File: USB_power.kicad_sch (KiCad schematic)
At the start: 29 parts, among them J1 PWR_IN, J2 USB_A_Stacked, J3 Power_check, J4 USB_C_Receptacle_USB2.0_16P, J5 USB_A

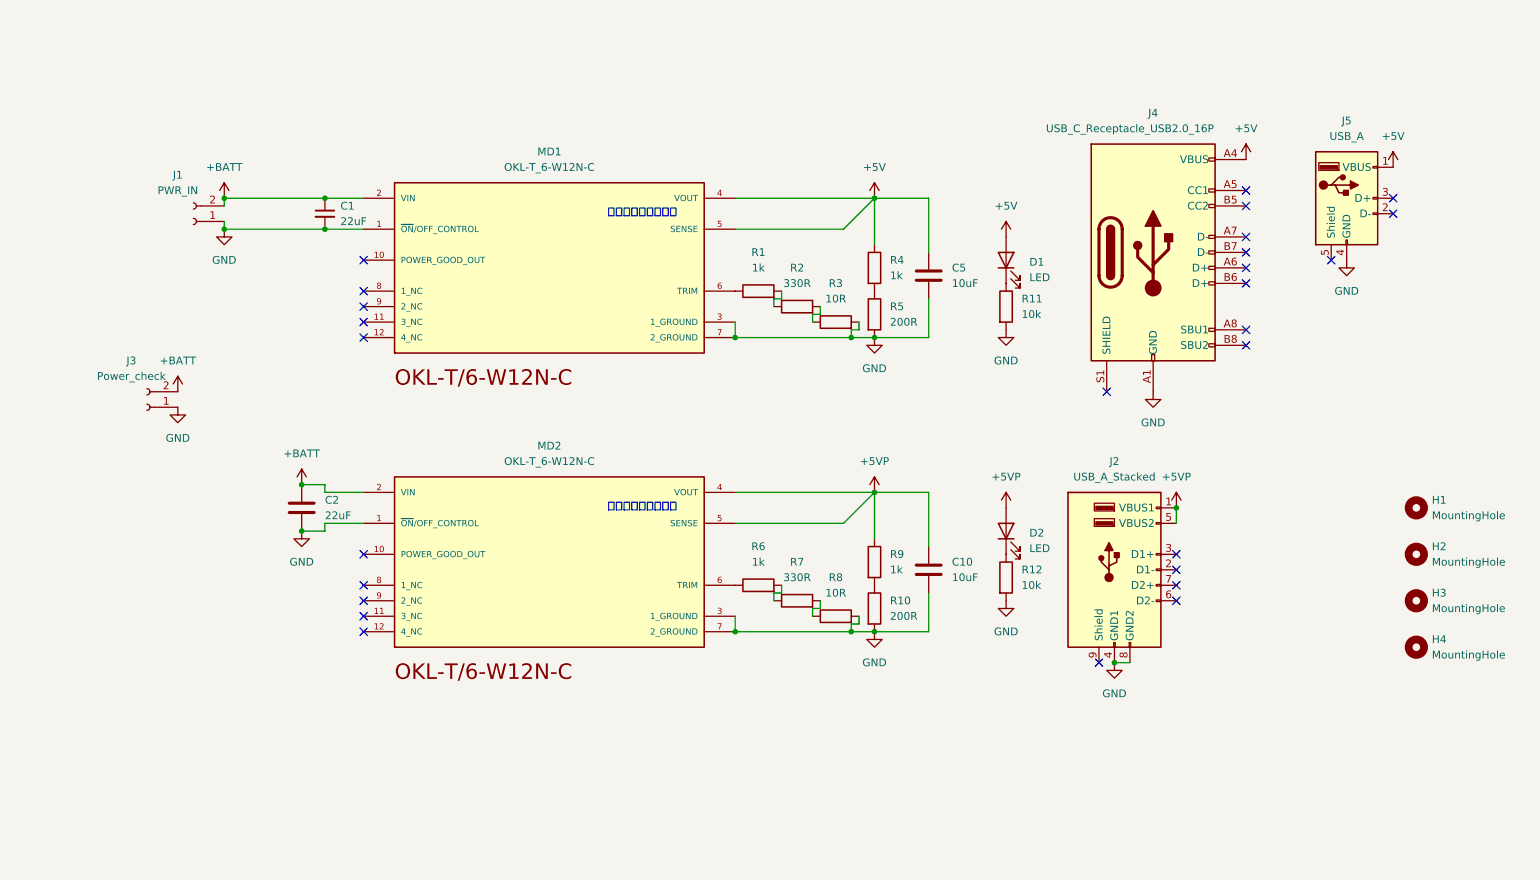
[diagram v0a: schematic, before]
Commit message: スケッチ見た目調整
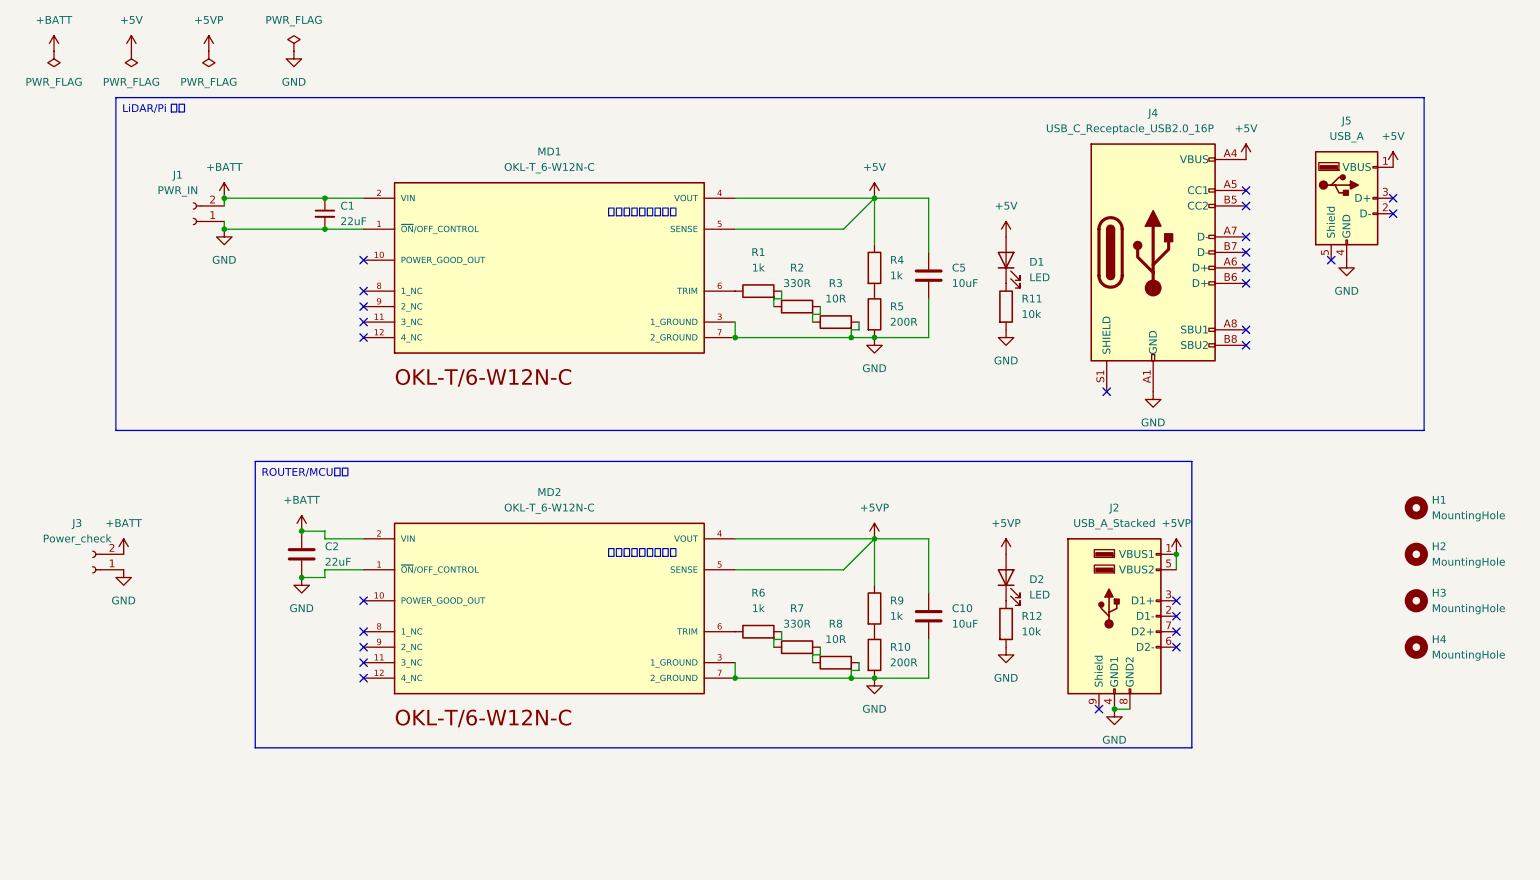
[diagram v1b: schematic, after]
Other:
- moved on the sheet: C10, C2, D2, J2, J3, MD2, R10, R12, R6, R7, R8, R9

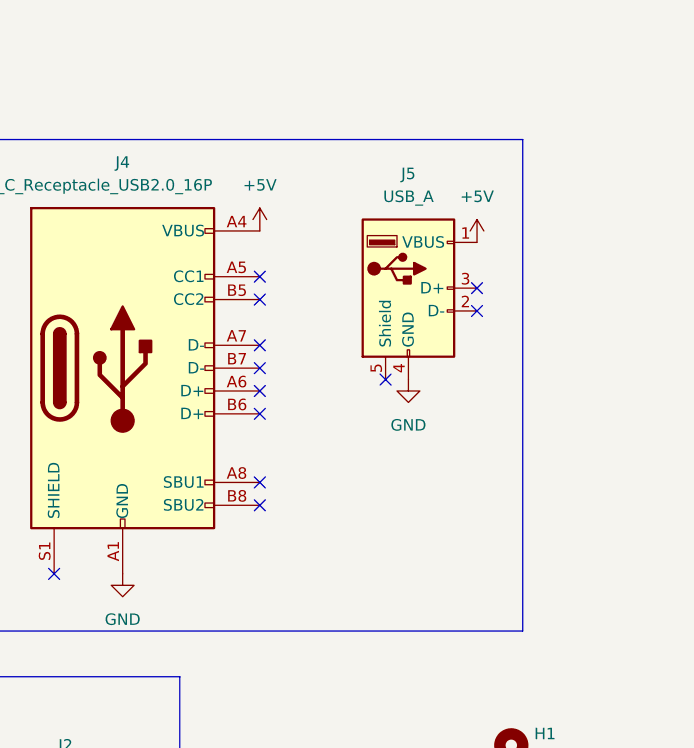
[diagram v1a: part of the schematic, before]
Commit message: SCH: MD1系統スタックコネクタに変更
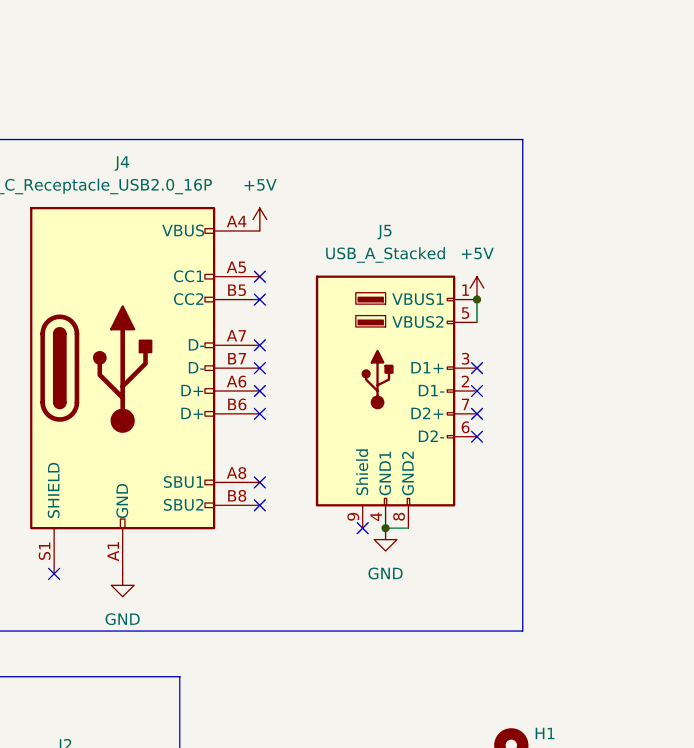
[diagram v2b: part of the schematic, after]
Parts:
- removed J5: USB_A, Connector_USB:USB_A_CONNFLY_DS1095-WNR0, symbol Connector:USB_A
- added J5: USB_A_Stacked, Connector_USB:USB_A_CUI_UJ2-ADH-TH_Horizontal_Stacked, symbol Connector:USB_A_Stacked
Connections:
- net +5V: now also J5.1 (VBUS1), J5.5 (VBUS2)
- net GND: now also J5.4 (GND1), J5.8 (GND2)
- no-connect marks 27 -> 29

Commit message: SCH: 不本意にもヒューズを追加
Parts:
- added F1: Fuse, FUSE_3557:FUSE_3557-2, symbol Device:Fuse
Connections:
- net +BATT: now also F1.1; no longer C1.1, MD1.2 (VIN)
- new net: C1.1, F1.2, MD1.2 (VIN)
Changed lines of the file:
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@@
+	)
+	(junction
+		(at 52.07 59.69)
+		(diameter 0)
+		(color 0 0 0 0)
 	)
 	(junction
@@
 	)
 	(junction
-		(at 52.07 59.69)
-		(diameter 0)
-		(color 0 0 0 0)
-	)
-	(junction
 		(at 64.77 121.92)
 		(diameter 0)
@@
 	)
 	(junction
-		(at 158.75 115.57)
+		(at 68.58 59.69)
 		(diameter 0)
 		(color 0 0 0 0)
 	)
 	(junction
-		(at 68.58 59.69)
+		(at 158.75 115.57)
 		(diameter 0)
 		(color 0 0 0 0)
@@
 	(wire
 		(pts
+			(xy 63.5 59.69) (xy 68.58 59.69)
+		)
+		(stroke
+			(width 0)
+			(type default)
+		)
+	)
+	(wire
+		(pts
 			(xy 167.64 76.2) (xy 167.64 82.55)
 		)
@@
 	(wire
 		(pts
-			(xy 52.07 59.69) (xy 68.58 59.69)
+			(xy 52.07 59.69) (xy 55.88 59.69)
 		)
 		(stroke
@@
 					(unit 1)
 				)
+			)
+		)
+	)
+	(symbol
+		(lib_id "Device:Fuse")
+		(at 59.69 59.69 90)
+		(unit 1)
+		(exclude_from_sim no)
+		(in_bom yes)
+		(on_board yes)
+		(dnp no)
+		(fields_autoplaced yes)
+		(property "Reference" "F1"
+			(at 59.69 53.34 90)
+			(effects
+				(font
+					(size 1.27 1.27)
+				)
+			)
+		)
+		(property "Value" "Fuse"
+			(at 59.69 55.88 90)
+			(effects
+				(font
+					(size 1.27 1.27)
+				)
+			)
+		)
+		(property "Footprint" "FUSE_3557:FUSE_3557-2"
+			(at 59.69 61.468 90)
+			(effects
+				(font
+					(size 1.27 1.27)
+				)
+				(hide yes)
+			)
+		)
+		(property "Datasheet" "~"
+			(at 59.69 59.69 0)
+			(effects
+				(font
+					(size 1.27 1.27)
+				)
+				(hide yes)
+			)
+		)
+		(property "Description" "Fuse"
+			(at 59.69 59.69 0)
+			(effects
+				(font
+					(size 1.27 1.27)
+				)
+				(hide yes)
+			)
+		)
+		(pin "1"
+		)
+		(pin "2"
+		)
+		(instances
+			(project ""
+				(path "/9b31bb12-b0a4-46c2-8fe3-73cecf9f3124"
+					(reference "F1")
+					(unit 1)
+				)

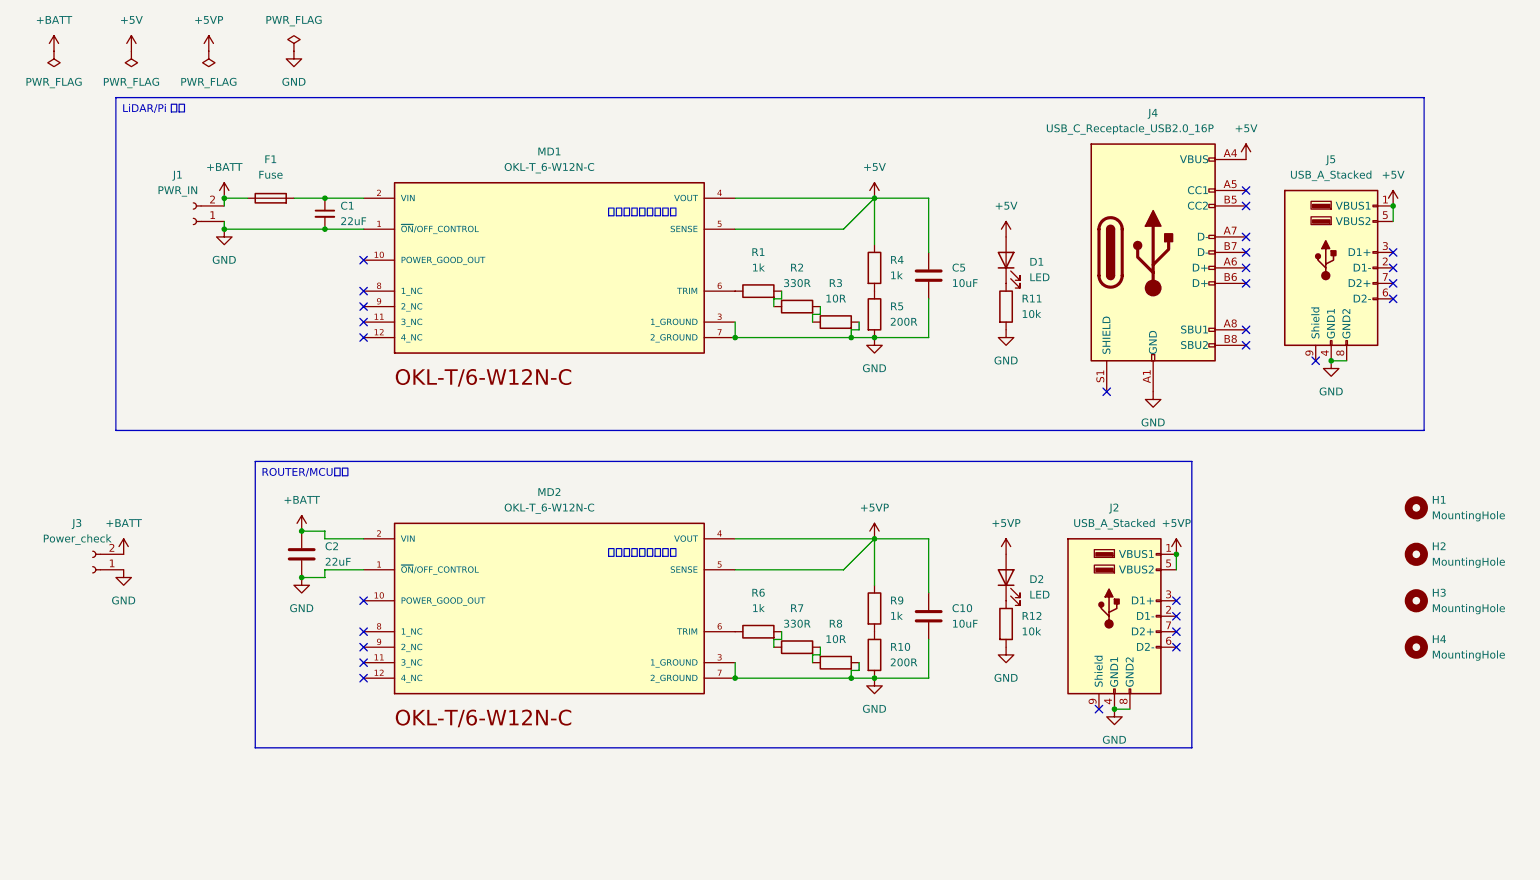
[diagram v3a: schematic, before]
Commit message: ヒューズ追加、外形削除
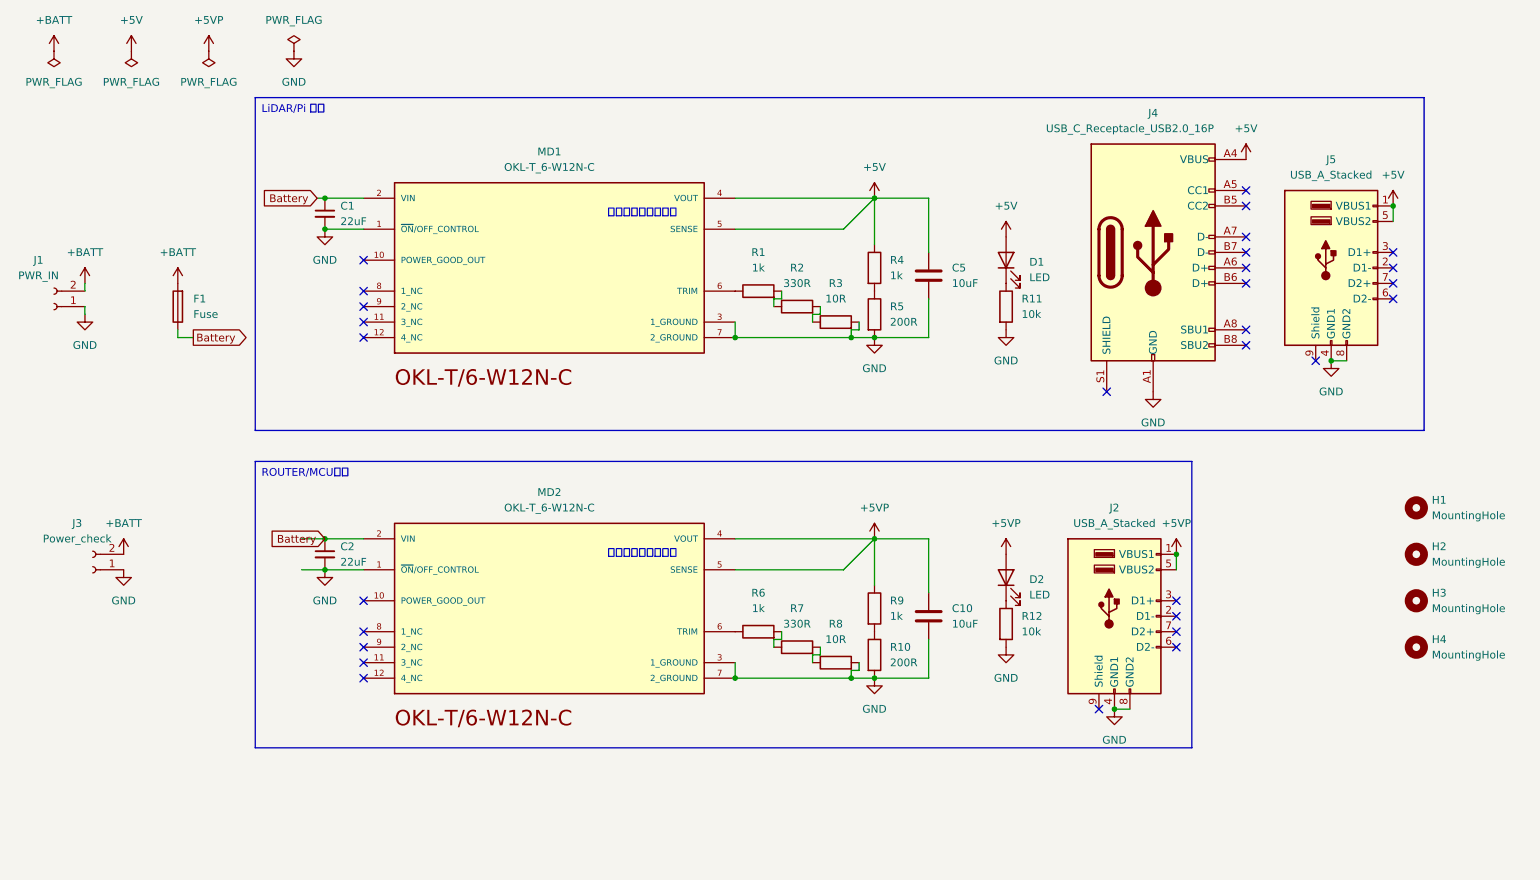
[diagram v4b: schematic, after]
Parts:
- C2: symbol Device:C -> Device:C_Small
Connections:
- net +BATT: now also F1.2; no longer C2.1, F1.1, MD2.2 (VIN)
- net Battery: now reaches C1.1, MD1.2 (VIN)
- net Battery: now also C2.1, F1.1, MD2.2 (VIN); no longer F1.2
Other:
- moved on the sheet: C2, F1, J1

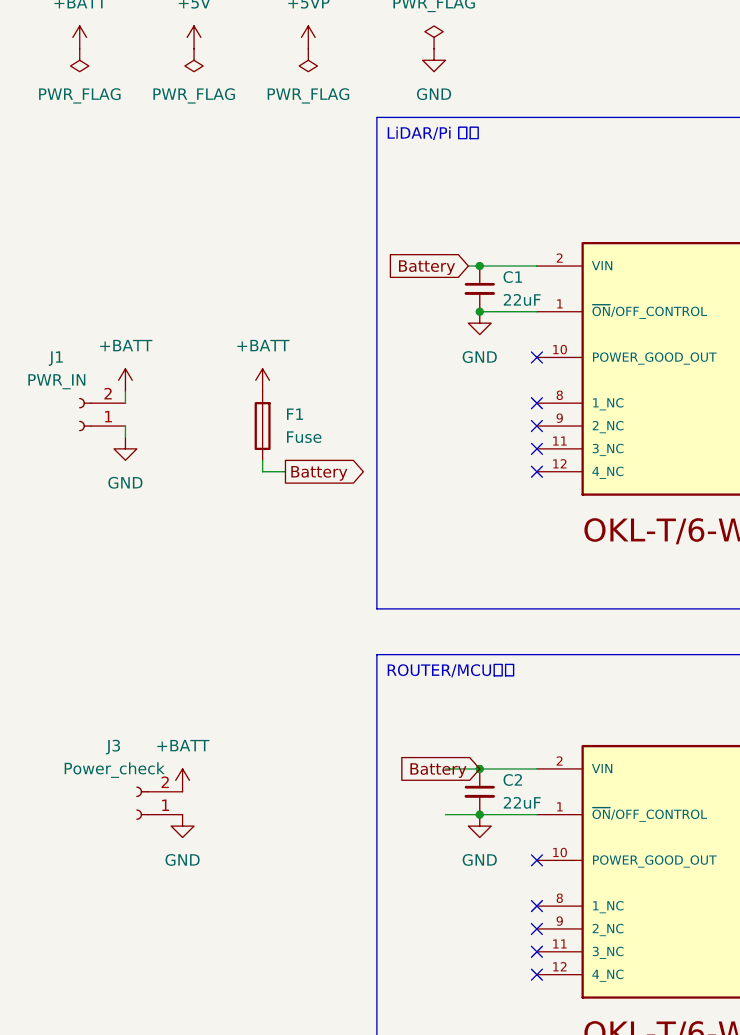
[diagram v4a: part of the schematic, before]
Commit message: スイッチと分圧抵抗配置
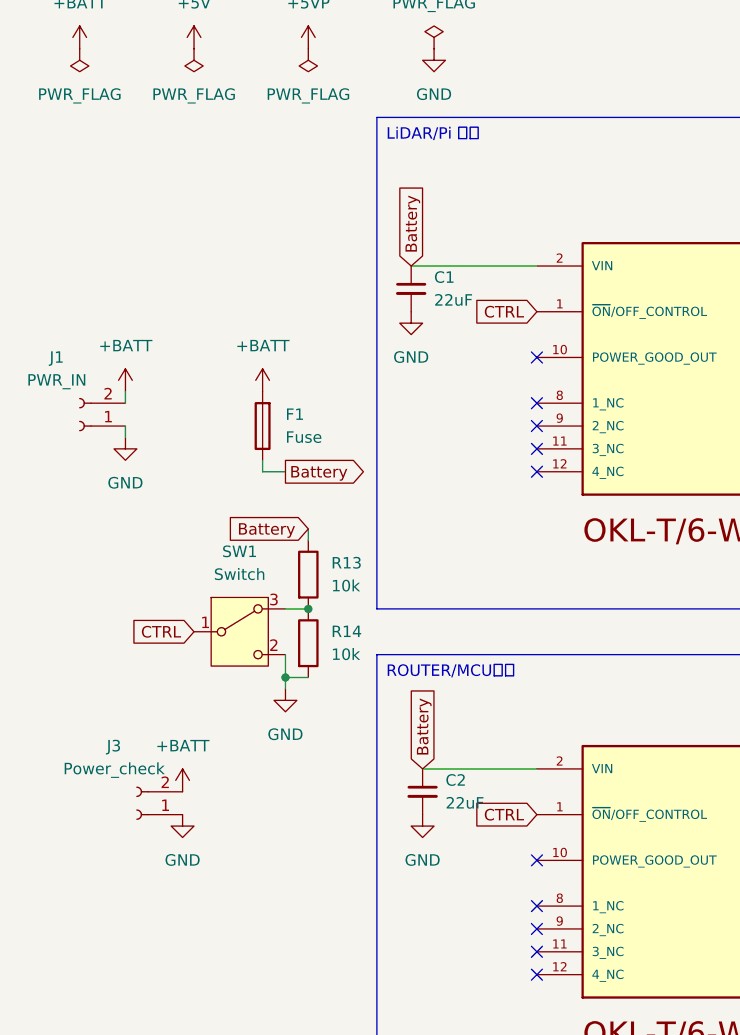
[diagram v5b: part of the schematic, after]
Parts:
- added R13, R14: 10k, Resistor_SMD:R_0805_2012Metric, symbol Device:R
- added SW1: Switch, Button_Switch_THT:SW_Slide-03_Wuerth-WS-SLTV_10x2.5x6.4_P2.54mm, symbol Switch:SW_Wuerth_450301014042
- H1, H2, H3, H4: footprint MountingHole:MountingHole_3.2mm_M3 -> MountingHole:MountingHole_3.2mm_M3_Pad_Via
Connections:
- net Battery: now also R13.1
- net GND: now also R14.2, SW1.2 (C); no longer MD1.1 (~{ON}/OFF_CONTROL), MD2.1 (~{ON}/OFF_CONTROL)
- new net: R13.2, R14.1, SW1.3 (A)
- new net CTRL: MD1.1 (~{ON}/OFF_CONTROL), MD2.1 (~{ON}/OFF_CONTROL), SW1.1 (B)
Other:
- moved on the sheet: C1, C2
